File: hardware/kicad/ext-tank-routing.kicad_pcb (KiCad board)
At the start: 2 copper layers, 120 x 80 mm, 16 parts, among them K201 G6K-2F-Y-DC5, K202 G6K-2F-Y-DC5, K203 G6K-2F-Y-DC5, K204 G6K-2F-Y-DC5, P201 JIO-WETSEND, P202 JTR-PRI, P203 JTR-SEC, P204 JTR-XFADE, P205 JFB-INJ, P206 JER-CTRL, P207 JER-PWR, U201 OPA1679IDR

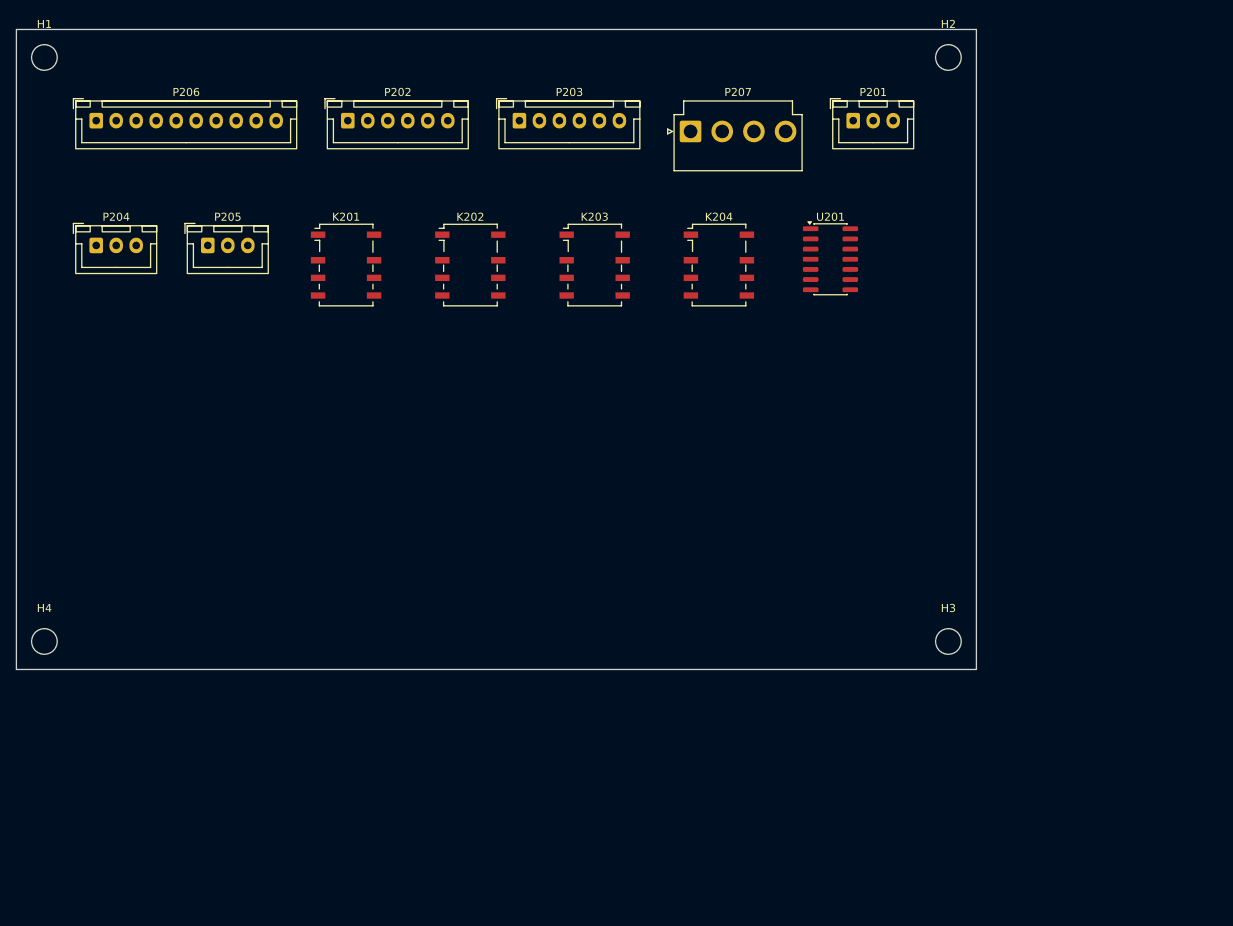
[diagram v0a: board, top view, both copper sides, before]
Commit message: Board 5 ext-tank-routing: ERC 0, sim verified (Series/Off relay modes, summers exact), routed DRC 0/0, fab outputs; relays standardized to G5V-2 DC5
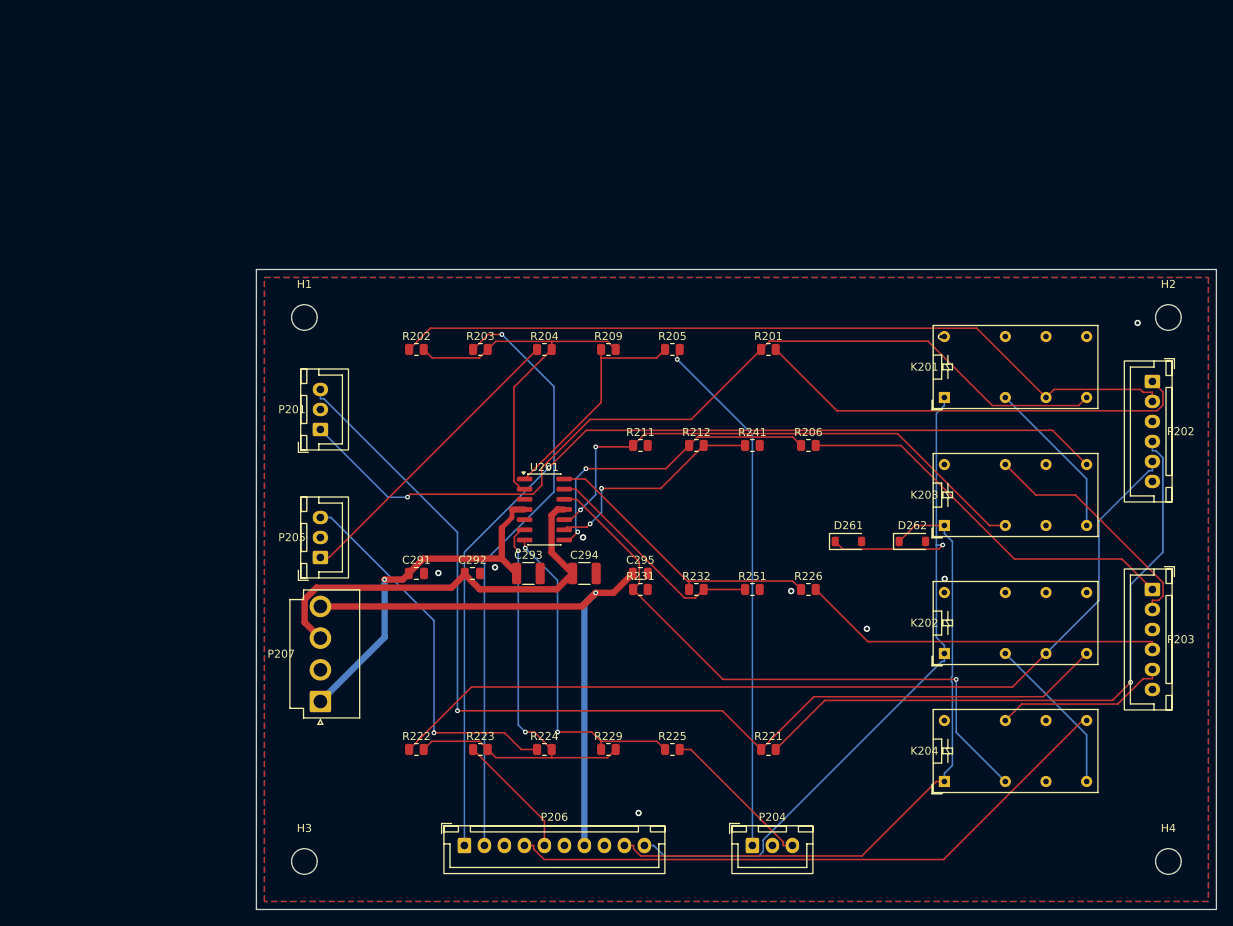
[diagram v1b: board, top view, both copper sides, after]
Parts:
- added C291: 100n, Capacitor_SMD:C_0805_2012Metric, F.Cu at (50.0, 68.0)
- added C292: 100n, Capacitor_SMD:C_0805_2012Metric, F.Cu at (57.0, 68.0)
- added C293: 22u, Capacitor_SMD:C_1210_3225Metric, F.Cu at (64.0, 68.0)
- added C294: 22u, Capacitor_SMD:C_1210_3225Metric, F.Cu at (71.0, 68.0)
- added C295: 100n, Capacitor_SMD:C_0805_2012Metric, F.Cu at (78.0, 68.0)
- added D261: 1N4148W, Diode_SMD:D_SOD-123, F.Cu at (104.0, 64.0)
- added D262: 1N4148W, Diode_SMD:D_SOD-123, F.Cu at (112.0, 64.0)
- added R201: 100, Resistor_SMD:R_0805_2012Metric, F.Cu at (94.0, 40.0)
- added R202: 20k, Resistor_SMD:R_0805_2012Metric, F.Cu at (50.0, 40.0)
- added R203: 20k, Resistor_SMD:R_0805_2012Metric, F.Cu at (58.0, 40.0)
- added R204: 20k, Resistor_SMD:R_0805_2012Metric, F.Cu at (66.0, 40.0)
- added R205: 100, Resistor_SMD:R_0805_2012Metric, F.Cu at (82.0, 40.0)
- added R206: 100, Resistor_SMD:R_0805_2012Metric, F.Cu at (99.0, 52.0)
- added R209: 20k, Resistor_SMD:R_0805_2012Metric, F.Cu at (74.0, 40.0)
- added R211: 100k, Resistor_SMD:R_0805_2012Metric, F.Cu at (78.0, 52.0)
- added R212: 0, Resistor_SMD:R_0805_2012Metric, F.Cu at (85.0, 52.0)
- added R221: 100, Resistor_SMD:R_0805_2012Metric, F.Cu at (94.0, 90.0)
- added R222: 20k, Resistor_SMD:R_0805_2012Metric, F.Cu at (50.0, 90.0)
- added R223: 20k, Resistor_SMD:R_0805_2012Metric, F.Cu at (58.0, 90.0)
- added R224: 20k, Resistor_SMD:R_0805_2012Metric, F.Cu at (66.0, 90.0)
- added R225: 100, Resistor_SMD:R_0805_2012Metric, F.Cu at (82.0, 90.0)
- added R226: 100, Resistor_SMD:R_0805_2012Metric, F.Cu at (99.0, 70.0)
- added R229: 20k, Resistor_SMD:R_0805_2012Metric, F.Cu at (74.0, 90.0)
- added R231: 100k, Resistor_SMD:R_0805_2012Metric, F.Cu at (78.0, 70.0)
- added R232: 0, Resistor_SMD:R_0805_2012Metric, F.Cu at (85.0, 70.0)
- added R241: 20k, Resistor_SMD:R_0805_2012Metric, F.Cu at (92.0, 52.0)
- added R251: 20k, Resistor_SMD:R_0805_2012Metric, F.Cu at (92.0, 70.0)
- H1, H2, H3, H4: value M3 NPTH -> M3; footprint MountingHole_3.2mm_M3 -> MountingHole:MountingHole_3.2mm_M3
- K201, K202, K203, K204: value G6K-2F-Y-DC5 -> G5V-2 DC5; footprint Relay_DPDT_Omron_G6K-2F-Y -> Relay_THT:Relay_DPDT_Omron_G5V-2
- P201: value JIO-WETSEND -> P201; footprint JST_XH_B3B-XH-A_1x03_P2.50mm_Vertical -> Connector_JST:JST_XH_B3B-XH-A_1x03_P2.50mm_Vertical
- P202: value JTR-PRI -> P202; footprint JST_XH_B6B-XH-A_1x06_P2.50mm_Vertical -> Connector_JST:JST_XH_B6B-XH-A_1x06_P2.50mm_Vertical
- P203: value JTR-SEC -> P203; footprint JST_XH_B6B-XH-A_1x06_P2.50mm_Vertical -> Connector_JST:JST_XH_B6B-XH-A_1x06_P2.50mm_Vertical
- P204: value JTR-XFADE -> P204; footprint JST_XH_B3B-XH-A_1x03_P2.50mm_Vertical -> Connector_JST:JST_XH_B3B-XH-A_1x03_P2.50mm_Vertical
- P205: value JFB-INJ -> P205; footprint JST_XH_B3B-XH-A_1x03_P2.50mm_Vertical -> Connector_JST:JST_XH_B3B-XH-A_1x03_P2.50mm_Vertical
- P206: value JER-CTRL -> P206; footprint JST_XH_B10B-XH-A_1x10_P2.50mm_Vertical -> Connector_JST:JST_XH_B10B-XH-A_1x10_P2.50mm_Vertical
- P207: value JER-PWR -> P207; footprint JST_VH_B4P-VH_1x04_P3.96mm_Vertical -> Connector_JST:JST_VH_B4P-VH_1x04_P3.96mm_Vertical
- U201: footprint SOIC-14_3.9x8.7mm_P1.27mm -> Package_SO:SOIC-14_3.9x8.7mm_P1.27mm
- moved H4 143.2 mm to (144.0, 104.0)
- moved P204 111.1 mm to (92.0, 102.0)
- moved P202 105.7 mm to (142.0, 44.0), turned to -90 degrees
- moved P206 101.6 mm to (56.0, 102.0)
- moved P203 98.5 mm to (142.0, 70.0), turned to -90 degrees
- moved H3 85.1 mm to (36.0, 104.0)
- moved P207 85.0 mm to (38.0, 84.0), turned to 90 degrees
- moved P201 77.0 mm to (38.0, 50.0), turned to 90 degrees
- moved K202 76.6 mm to (116.0, 78.0), turned to 90 degrees
- moved K201 76.6 mm to (116.0, 46.0), turned to 90 degrees
- moved K204 70.4 mm to (116.0, 94.0), turned to 90 degrees
- moved K203 54.5 mm to (116.0, 62.0), turned to 90 degrees
- moved U201 47.5 mm to (66.0, 60.0)
- moved H1 46.0 mm to (36.0, 36.0)
- moved H2 42.6 mm to (144.0, 36.0)
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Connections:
- K201 pad 1: (no net) -> CTL_EXT_MODE_B
- K201 pad 4: (no net) -> SEC_SEL_L
- K201 pad 6: (no net) -> PRI_RET_L
- K201 pad 8: (no net) -> WET_SEND_L
- K202 pad 1: (no net) -> CTL_EXT_MODE_B
- K202 pad 4: (no net) -> SEC_SEL_R
- K202 pad 6: (no net) -> PRI_RET_R
- K202 pad 8: (no net) -> WET_SEND_R
- K203 pad 1: (no net) -> CTL_EXT_MODE_A
- K203 pad 4: (no net) -> SEC_DRV_L
- K203 pad 8: (no net) -> SEC_SEL_L
- K204 pad 1: (no net) -> CTL_EXT_MODE_A
- K204 pad 4: (no net) -> SEC_DRV_R
- K204 pad 8: (no net) -> SEC_SEL_R
- P201 pad 1: (no net) -> WET_SEND_L
- P201 pad 2: (no net) -> AGND
- P201 pad 3: (no net) -> WET_SEND_R
- P202 pad 1: (no net) -> PRI_SEND_L
- P202 pad 2: (no net) -> PRI_RET_L
- P202 pad 3: (no net) -> AGND
- P202 pad 4: (no net) -> PRI_SEND_R
- P202 pad 5: (no net) -> PRI_RET_R
- P202 pad 6: (no net) -> AGND
- P203 pad 1: (no net) -> SEC_SEND_L
- P203 pad 2: (no net) -> SEC_RET_L
- P203 pad 3: (no net) -> AGND
- P203 pad 4: (no net) -> SEC_SEND_R
- P203 pad 5: (no net) -> SEC_RET_R
- P203 pad 6: (no net) -> AGND
- P204 pad 1: (no net) -> TANK_MIX_L
- P204 pad 2: (no net) -> AGND
- P204 pad 3: (no net) -> TANK_MIX_R
- P205 pad 1: (no net) -> FB_RET_L
- P205 pad 2: (no net) -> AGND
- P205 pad 3: (no net) -> FB_RET_R
- P206 pad 1: (no net) -> EXTMIX_L_HI
- P206 pad 10: (no net) -> CTL_EXT_MODE_B
- P206 pad 2: (no net) -> EXTMIX_L_WIPER
- P206 pad 3: (no net) -> AGND
- P206 pad 4: (no net) -> EXTMIX_R_HI
- P206 pad 5: (no net) -> EXTMIX_R_WIPER
- P206 pad 6: (no net) -> AGND
- P206 pad 7: (no net) -> +5VAUX
- P206 pad 8: (no net) -> AGND
- P206 pad 9: (no net) -> CTL_EXT_MODE_A
- P207 pad 1: (no net) -> +15VA
- P207 pad 2: (no net) -> AGND
- P207 pad 3: (no net) -> -15VA
- P207 pad 4: (no net) -> +5VAUX
- U201 pad 1: (no net) -> N_TMIX_L
- U201 pad 10: (no net) -> SEC_DRV_L
- U201 pad 11: (no net) -> -15VA
- U201 pad 12: (no net) -> SEC_DRV_R
- U201 pad 13: (no net) -> N_SECFB_R
- U201 pad 14: (no net) -> N_SECBUF_R
- U201 pad 2: (no net) -> N_SUM_L_M
- U201 pad 3: (no net) -> AGND
- U201 pad 4: (no net) -> +15VA
- U201 pad 5: (no net) -> AGND
- U201 pad 6: (no net) -> N_SUM_R_M
- U201 pad 7: (no net) -> N_TMIX_R
- U201 pad 8: (no net) -> N_SECBUF_L
- U201 pad 9: (no net) -> N_SECFB_L
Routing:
- net WET_SEND_R: track 0.00 -> 133.1 mm, vias 0 -> 1
- net EXTMIX_L_HI: track 0.00 -> 122.5 mm, vias 0 -> 1
- net PRI_RET_R: track 0.00 -> 114.3 mm
- net WET_SEND_L: track 0.00 -> 112.4 mm, vias 0 -> 1
- net PRI_RET_L: track 0.00 -> 99.3 mm
- net CTL_EXT_MODE_B: track 0.00 -> 97.6 mm, vias 0 -> 1
- net CTL_EXT_MODE_A: track 0.00 -> 84.1 mm
- net PRI_SEND_R: track 0.00 -> 80.4 mm, vias 0 -> 1
- net EXTMIX_R_HI: track 0.00 -> 78.5 mm
- net SEC_DRV_R: track 0.00 -> 76.8 mm, vias 0 -> 1
- net EXTMIX_L_WIPER: track 0.00 -> 74.5 mm, vias 0 -> 1
- net +5VAUX: track 0.00 -> 72.9 mm, vias 0 -> 1
- net SEC_DRV_L: track 0.00 -> 67.9 mm, vias 0 -> 2
- net TANK_MIX_L: track 0.00 -> 66.0 mm, vias 0 -> 1
- net N_SUM_R_M: track 0.00 -> 57.5 mm, vias 0 -> 2
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- added copper zone on B.Cu, net AGND
- added copper zone on F.Cu, net AGND
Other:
- board text removed: "GAS Rev A - External Tank Routing Board"
- board text removed: "OUTLINE SCAFFOLD - NOT FOR FAB"

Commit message: ext-tank-routing: move feedback reinjection pre-tank (U202 send summers)
FB_RET_L/R now sum with WET_SEND_L/R at new OPA1656 send summers (U202)
upstream of PRI_SEND and the parallel-mode pickoff, so feedback re-passes
through the spring tanks. Removed FB_RET from the U201A/B TANK_MIX output
summers. Matches the JUCE sim, where feedbackReturnBuffer adds into
wetInputBaseBuffer before predelay+convolution (= the tanks).

- gen_ext.py: U202 stage, R207/R208/R227/R228 20k, C296/C297 100n,
  K201/K202 parallel contact now picks SEND_MIX; OPA1656 sim model added
- route_board.py: ext board routes AGND as a net (pour-only stranded
  U201 pad 5)
- ERC 0, tran sim verified (FB reaches PRI_SEND, absent from TANK_MIX),
  DRC 0 errors / 0 unconnected; fab packet regenerated
- docs: interfaces.md, ext-routing + crossfade schematic-ready defs,
  board doc, harness map, BOMs, order-readiness
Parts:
- removed the R201 at (94.0, 40.0)
- removed the R202 at (50.0, 40.0)
- added D262: 1N4148W, Diode_SMD:D_SOD-123, F.Cu at (112.0, 64.0)
- added H1: M3, MountingHole:MountingHole_3.2mm_M3, F.Cu at (36.0, 36.0)
- added K201: G5V-2 DC5, Relay_THT:Relay_DPDT_Omron_G5V-2, F.Cu at (116.0, 46.0)
- added R229: 20k, Resistor_SMD:R_0805_2012Metric, F.Cu at (66.0, 90.0)
- added R231: 100k, Resistor_SMD:R_0805_2012Metric, F.Cu at (78.0, 70.0)
- added R232: 0, Resistor_SMD:R_0805_2012Metric, F.Cu at (85.0, 70.0)
- added R241: 20k, Resistor_SMD:R_0805_2012Metric, F.Cu at (92.0, 52.0)
- added U201: OPA1679IDR, Package_SO:SOIC-14_3.9x8.7mm_P1.27mm, F.Cu at (66.0, 60.0)
- added U202: OPA1656IDR, Package_SO:SOIC-8_3.9x4.9mm_P1.27mm, F.Cu at (52.0, 52.0)
- C296: renamed from D261; value 1N4148W -> 100n; footprint Diode_SMD:D_SOD-123 -> Capacitor_SMD:C_0805_2012Metric
- C297: renamed from D262; value 1N4148W -> 100n; footprint Diode_SMD:D_SOD-123 -> Capacitor_SMD:C_0805_2012Metric
- D261: renamed from K201; value G5V-2 DC5 -> 1N4148W; footprint Relay_THT:Relay_DPDT_Omron_G5V-2 -> Diode_SMD:D_SOD-123
- R201: renamed from R203; value 20k -> 100
- R203: renamed from R205; value 100 -> 20k
- R204: renamed from R206; value 100 -> 20k
- R205: renamed from R209; value 20k -> 100
- R206: renamed from R211; value 100k -> 100
- R207: renamed from R212; value 0 -> 20k
- R208: renamed from R221; value 100 -> 20k
- R211: renamed from R223; value 20k -> 100k
- R212: renamed from R224; value 20k -> 0
- R222: renamed from R226; value 100 -> 20k
- R224: renamed from R231; value 100k -> 20k
- R225: renamed from R232; value 0 -> 100
- R226: renamed from R241; value 20k -> 100
- R228: renamed from U201; value OPA1679IDR -> 20k; footprint Package_SO:SOIC-14_3.9x8.7mm_P1.27mm -> Resistor_SMD:R_0805_2012Metric
- R251: renamed from H1; value M3 -> 20k; footprint MountingHole:MountingHole_3.2mm_M3 -> Resistor_SMD:R_0805_2012Metric
- moved R251 65.5 mm to (92.0, 70.0)
- moved R208 56.9 mm to (58.0, 46.0)
- moved R222 52.9 mm to (50.0, 90.0)
- moved R209 52.5 mm to (66.0, 40.0)
- moved R227 49.5 mm to (44.0, 58.0)
- moved R204 48.4 mm to (51.0, 46.0)
- moved R211 42.9 mm to (78.0, 52.0)
- moved R212 42.5 mm to (85.0, 52.0)
- moved R207 41.4 mm to (44.0, 46.0)
- moved R201 36.0 mm to (94.0, 40.0)
- moved R224 29.5 mm to (51.0, 58.0)
- moved R203 24.0 mm to (58.0, 40.0)
- moved R225 22.8 mm to (74.0, 90.0)
- moved D261 21.6 mm to (104.0, 64.0), turned to 0 degrees
- moved R206 21.0 mm to (99.0, 52.0)
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- renumbered R204 to R202, R222 to R209, R225 to R221, R229 to R223, R251 to R227
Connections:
- C296 pad 1: CTL_EXT_MODE_B -> +15VA
- C297 pad 1: CTL_EXT_MODE_A -> -15VA
- K202 pad 8: WET_SEND_R -> SEND_MIX_R
- R201 pad 1: EXTMIX_L_WIPER -> SEND_MIX_L
- R201 pad 2: N_SUM_L_M -> PRI_SEND_L
- R202 pad 1: FB_RET_L -> PRI_RET_L
- R203 pad 1: N_TMIX_L -> EXTMIX_L_WIPER
- R203 pad 2: TANK_MIX_L -> N_SUM_L_M
- R204 pad 1: N_SECBUF_L -> FB_RET_L
- R204 pad 2: SEC_SEND_L -> N_SND_L_M
- R205 pad 2: N_SUM_L_M -> TANK_MIX_L
- R206 pad 1: SEC_DRV_L -> N_SECBUF_L
- R206 pad 2: AGND -> SEC_SEND_L
- R207 pad 1: N_SECBUF_L -> WET_SEND_L
- R207 pad 2: N_SECFB_L -> N_SND_L_M
- R208 pad 1: WET_SEND_R -> SEND_MIX_L
- R208 pad 2: PRI_SEND_R -> N_SND_L_M
- R209 pad 1: PRI_RET_R -> N_TMIX_L
- R209 pad 2: N_SUM_R_M -> N_SUM_L_M
- R211 pad 1: EXTMIX_R_WIPER -> SEC_DRV_L
- R211 pad 2: N_SUM_R_M -> AGND
- R212 pad 1: FB_RET_R -> N_SECBUF_L
- R212 pad 2: N_SUM_R_M -> N_SECFB_L
- R221 pad 1: N_TMIX_R -> SEND_MIX_R
- R221 pad 2: TANK_MIX_R -> PRI_SEND_R
- R222 pad 1: N_SECBUF_R -> PRI_RET_R
- R222 pad 2: SEC_SEND_R -> N_SUM_R_M
- R223 pad 1: N_TMIX_R -> EXTMIX_R_WIPER
- R224 pad 1: SEC_DRV_R -> FB_RET_R
- R224 pad 2: AGND -> N_SND_R_M
- R225 pad 1: N_SECBUF_R -> N_TMIX_R
- R225 pad 2: N_SECFB_R -> TANK_MIX_R
- R226 pad 1: N_SECFB_L -> N_SECBUF_R
- R226 pad 2: AGND -> SEC_SEND_R
- R227 pad 1: N_SECFB_R -> WET_SEND_R
- R227 pad 2: AGND -> N_SND_R_M
- R228 pad 1: N_TMIX_L -> SEND_MIX_R
- R228 pad 2: N_SUM_L_M -> N_SND_R_M
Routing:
- net WET_SEND_R: track 133.1 -> 16.4 mm, vias 1 -> 0
- net SEND_MIX_L: track 0.00 -> 108.3 mm
- net WET_SEND_L: track 112.4 -> 6.74 mm, vias 1 -> 0
- net SEND_MIX_R: track 0.00 -> 105.0 mm, vias 0 -> 2
- net +15VA: track 45.2 -> 91.6 mm, vias 1 -> 0
- net -15VA: track 52.4 -> 90.2 mm, vias 0 -> 2
- net FB_RET_R: track 47.3 -> 17.0 mm
- net N_SND_R_M: track 0.00 -> 26.8 mm
- net N_SND_L_M: track 0.00 -> 21.4 mm
- net +5VAUX: track 72.9 -> 86.1 mm, vias 1 -> 0
- net N_SECBUF_R: track 36.4 -> 47.8 mm
- net N_SUM_R_M: track 57.5 -> 46.2 mm
- net N_SUM_L_M: track 46.9 -> 35.9 mm
- net EXTMIX_L_HI: track 122.5 -> 112.8 mm, vias 1 -> 0
- net FB_RET_L: track 37.9 -> 29.8 mm
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
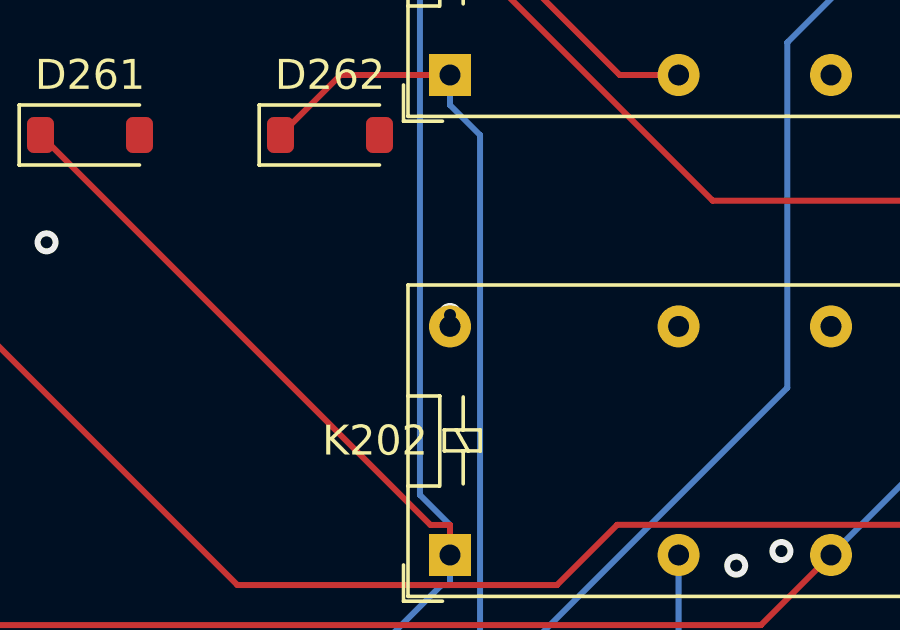
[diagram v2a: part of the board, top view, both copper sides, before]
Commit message: Order prep: HQDFM triage of all six boards, assembly BOMs, fab output fixes
- assembly-ready BOMs (bom-assembly.csv/.xlsx) merged from fab + priced BOMs with MPN/Manufacturer/Qty/DNP; J1-J4 corrected to board-mounted JST headers; xlsx centroid files for NextPCB upload
- HQDFM reports triaged for all six boards: all 'missing THT hole' flags verified false (drill files complete on all six), IPC open/shorts = absent netlist, power NPTH flag = noise
- filter-clipper: removed 9 duplicate drill hits (stacked AGND vias) from .drl and gerber zip, verified zero dups and full pad/via coverage; kicad_pcb dedupe deferred to rev B
- via-in-pad relocation evaluated and rejected (no compliant spot within 3.2mm); accepted for rev A, logged with full rev-B punch list in rev-a-open-issues.md item 0
- all-boards gerber bundle zip for convenience (not for upload)
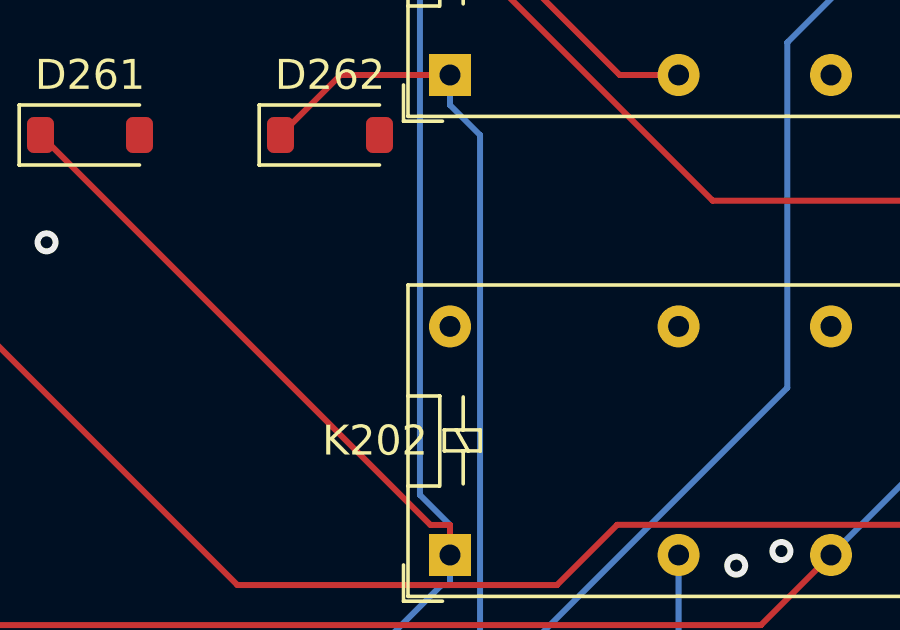
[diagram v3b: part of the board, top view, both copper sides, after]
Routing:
- net AGND: vias 31 -> 30
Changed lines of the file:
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@@
-	)
-	(via
-		(at 115.999999 69.999999)
-		(size 0.8)
-		(drill 0.4)
-		(layers "F.Cu" "B.Cu")
-		(net "AGND")
 	)
 	(via
